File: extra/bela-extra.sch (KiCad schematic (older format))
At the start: 15 parts, among them P1 bbbp9, P14 ext_power, P2 bbbp8, P3 enc+btn1, P4 enc+btn2, P5 MTA-156-2, P6 bela_power, U2 7805-xnor

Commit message: working with enables on extra board
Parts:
- removed C1: 220uF, Capacitors_ThroughHole:C_Radial_D5_L11_P2, symbol CP
- removed C6: 47uF, Capacitors_ThroughHole:C_Radial_D5_L11_P2, symbol CP
- removed D1: 1N5400, Diodes_ThroughHole:Diode_DO-41_SOD81_Horizontal_RM10, symbol D
- removed P1: bbbp9, Pin_Headers:Pin_Header_Straight_2x08_Pitch2.54mm, symbol CONN_02X08
- removed P6: bela_power, mta-156:MTA-156-2, symbol CONN_01X02
- removed R4: bead, xnorman:Resistor_Vertical_RM5mm-xnor, symbol R
- removed U2: 7805-xnor, TO_SOT_Packages_THT:TO-220_Neutral123_Vertical_LargePads, symbol 7805-xnor
- added P1: bbbp9, Pin_Headers:Pin_Header_Straight_2x23_Pitch2.54mm, symbol CONN_02X23
- added R?: bead, xnorman:Resistor_Vertical_RM5mm-xnor, symbol R
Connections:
- net 5v: now also R?.2
- net beladigin6: no longer P2.12 (P12)
- net encin1-a: no longer P2.24 (P24)
- net encin1-b: no longer P2.22 (P22)
- net encin1-btn: no longer P2.20 (P20)
- net encin2-a: now also P1.16 (P16)
- net encin2-b: now also P1.14 (P14)
- net encin2-btn: now also P1.12 (P12)
- net bb-vfdCTRLenable: now reaches P2.14 (P14)
- net at R1.2: now also P1.4 (P4)
- net bb-vfdD7enable: no longer names the net of P2.32 (P32)
- new net: P1.5 (P5), R?.1
- new net bb-vfdDOUTenable: P2.12 (P12)
- no-connect marks 25 -> 23
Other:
- note added: "26 used by bela"
- note added: "WHY DIDN't Bela USE GPIO_26 Pin 14 for digital/io???? seems good.."
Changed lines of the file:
@@
 Text GLabel 9650 1250 2    60   Output ~ 0
 +15v
-$Comp
-L R R4
-U 1 1 58571EBD
-P 10350 3150
-F 0 "R4" V 10430 3150 50  0000 C CNN
-F 1 "bead" V 10350 3150 50  0000 C CNN
-F 2 "xnorman:Resistor_Vertical_RM5mm-xnor" V 10280 3150 50  0001 C CNN
-F 3 "" H 10350 3150 50  0000 C CNN
-	1    10350 3150
-	0    1    1    0
-$EndComp
-$Comp
-L CP C6
-U 1 1 58571F15
-P 9900 3350
-F 0 "C6" H 9925 3450 50  0000 L CNN
-F 1 "47uF" H 9925 3250 50  0000 L CNN
-F 2 "Capacitors_ThroughHole:C_Radial_D5_L11_P2" H 9938 3200 50  0001 C CNN
-F 3 "" H 9900 3350 50  0000 C CNN
-	1    9900 3350
-	1    0    0    -1
-$EndComp
-$Comp
-L CP C1
-U 1 1 58571F59
-P 8750 3350
-F 0 "C1" H 8775 3450 50  0000 L CNN
-F 1 "220uF" H 8775 3250 50  0000 L CNN
-F 2 "Capacitors_ThroughHole:C_Radial_D5_L11_P2" H 8788 3200 50  0001 C CNN
-F 3 "" H 8750 3350 50  0000 C CNN
-	1    8750 3350
-	1    0    0    -1
-$EndComp
-$Comp
-L D D1
-U 1 1 58571F9F
-P 8400 3150
-F 0 "D1" H 8400 3250 50  0000 C CNN
-F 1 "1N5400" H 8400 3050 50  0000 C CNN
-F 2 "Diodes_ThroughHole:Diode_DO-41_SOD81_Horizontal_RM10" H 8400 3150 50  0001 C CNN
-F 3 "" H 8400 3150 50  0000 C CNN
-	1    8400 3150
-	-1   0    0    -1
-$EndComp
-Text GLabel 7900 3150 0    60   Input ~ 0
-+15v
-$Comp
-L GND #PWR02
-U 1 1 58572336
-P 9200 3750
-F 0 "#PWR02" H 9200 3500 50  0001 C CNN
-F 1 "GND" H 9200 3600 50  0000 C CNN
-F 2 "" H 9200 3750 50  0000 C CNN
-F 3 "" H 9200 3750 50  0000 C CNN
-	1    9200 3750
-	1    0    0    -1
-$EndComp
-Text GLabel 10050 2950 1    60   Output ~ 0
-5v
-$Comp
-L CONN_01X02 P6
-U 1 1 58577BC4
-P 10800 3550
-F 0 "P6" H 10800 3700 50  0000 C CNN
-F 1 "bela_power" V 10900 3550 50  0000 C CNN
-F 2 "mta-156:MTA-156-2" H 10800 3550 50  0001 C CNN
-F 3 "" H 10800 3550 50  0000 C CNN
-	1    10800 3550
-	1    0    0    -1
-$EndComp
 $Sheet
 S 2300 650  1400 1350
@@
 	1    0    0    -1
 $EndComp
-Text GLabel 5300 5200 2    60   Output ~ 0
-bb-vfdD7enable
+Text GLabel 5300 4200 2    60   Output ~ 0
+bb-vfdDOUTenable
 Text GLabel 5350 5900 2    60   Output ~ 0
 bb-vfdD0
@@
 Text GLabel 4700 4200 0    60   Input ~ 0
 beladigin5
-Text GLabel 5300 4200 2    60   Input ~ 0
-beladigin6
 Text GLabel 5350 4400 2    60   Output ~ 0
 beladigout2
@@
 Text GLabel 5350 5100 2    60   Output ~ 0
 beladigout6
-Text GLabel 4700 5100 0    60   Output ~ 0
-beladigout7
 Text GLabel 2450 3800 2    60   Output ~ 0
 3.3v
@@
 Text GLabel 2150 4400 2    60   Input ~ 0
 encin2-a
-Text GLabel 5350 4700 2    60   Input ~ 0
+Text GLabel 6550 4400 2    60   Input ~ 0
 encin1-b
-Text GLabel 5350 4600 2    60   Input ~ 0
+Text GLabel 6550 4300 2    60   Input ~ 0
 encin1-btn
-Text GLabel 5350 4800 2    60   Input ~ 0
+Text GLabel 6550 4500 2    60   Input ~ 0
 encin1-a
-Text Notes 5900 4750 0    60   ~ 0
+Text Notes 7100 4450 0    60   ~ 0
 enc1 not mapped to bela digital
 Text Notes 2200 4100 0    60   ~ 0
@@
 NoConn ~ 1500 3700
 NoConn ~ 1500 3800
-NoConn ~ 1500 3900
 NoConn ~ 2000 3700
 NoConn ~ 2000 3900
@@
 NoConn ~ 5250 3800
 NoConn ~ 5250 3900
-NoConn ~ 5250 4300
 NoConn ~ 4750 4300
 NoConn ~ 4750 4500
@@
 NoConn ~ 5250 4900
 NoConn ~ 4750 5300
-$Comp
-L CONN_02X08 P1
-U 1 1 586DA958
-P 1750 4050
-F 0 "P1" H 1750 4500 50  0000 C CNN
-F 1 "bbbp9" V 1750 4050 50  0000 C CNN
-F 2 "Pin_Headers:Pin_Header_Straight_2x08_Pitch2.54mm" H 1750 2850 50  0001 C CNN
-F 3 "" H 1750 2850 50  0000 C CNN
-	1    1750 4050
-	1    0    0    -1
-$EndComp
 $Comp
 L PWR_FLAG #FLG05
@@
 $EndComp
 $Comp
-L 7805-xnor U2
-U 1 1 586E3B91
-P 9350 3200
-F 0 "U2" H 9500 3004 50  0000 C CNN
-F 1 "7805-xnor" H 9350 3400 50  0000 C CNN
-F 2 "TO_SOT_Packages_THT:TO-220_Neutral123_Vertical_LargePads" H 9350 3200 50  0001 C CNN
-F 3 "" H 9350 3200 50  0000 C CNN
-	1    9350 3200
-	1    0    0    -1
-$EndComp
-$Comp
 L PWR_FLAG #FLG06
 U 1 1 586F1ADD
@@
 	9350 1250 9650 1250
 Wire Wire Line
-	9350 3650 9350 3450
-Wire Wire Line
-	8750 3650 10000 3650
-Wire Wire Line
-	8750 3650 8750 3500
-Wire Wire Line
-	9900 3650 9900 3500
-Connection ~ 9350 3650
-Wire Wire Line
-	8550 3150 8950 3150
-Wire Wire Line
-	8750 3150 8750 3200
-Connection ~ 8750 3150
-Wire Wire Line
-	7900 3150 8250 3150
-Wire Wire Line
-	9200 3750 9200 3650
-Connection ~ 9200 3650
-Wire Wire Line
-	10550 3500 10600 3500
-Wire Wire Line
-	10600 3600 10000 3600
-Wire Wire Line
-	10000 3600 10000 3650
-Connection ~ 9900 3650
-Wire Wire Line
-	10500 3150 10550 3150
-Wire Wire Line
-	10550 3150 10550 3500
-Wire Wire Line
 	5250 3700 5800 3700
 Wire Wire Line
@@
 	5300 5300 5250 5300
 Wire Wire Line
-	5250 5200 5300 5200
-Wire Wire Line
 	4650 5200 4750 5200
 Wire Wire Line
@@
 Wire Wire Line
 	5250 4100 5300 4100
-Wire Wire Line
-	5250 4200 5300 4200
 Wire Wire Line
 	4700 4400 4750 4400
@@
 Wire Wire Line
 	2150 4400 2000 4400
-Wire Wire Line
-	5350 4600 5250 4600
-Wire Wire Line
-	5250 4700 5350 4700
-Wire Wire Line
-	5250 4800 5350 4800
 Connection ~ 9600 1250
 Wire Wire Line
@@
 Wire Wire Line
 	9600 1050 9600 1250
-Wire Wire Line
-	9750 3150 10200 3150
-Wire Wire Line
-	9900 3150 9900 3200
-Connection ~ 9900 3150
-Wire Wire Line
-	10050 2950 10050 3150
-Connection ~ 10050 3150
 Wire Wire Line
 	2400 3650 2400 3800
@@
 	-1   0    0    1
 $EndComp
+Text GLabel 5350 4300 2    60   Output ~ 0
+bb-vfdCTRLenable
+$Comp
+L CONN_02X23 P1
+U 1 1 589C11B1
+P 1750 4800
+F 0 "P1" H 1750 6000 50  0000 C CNN
+F 1 "bbbp9" V 1750 4800 50  0000 C CNN
+F 2 "Pin_Headers:Pin_Header_Straight_2x23_Pitch2.54mm" H 1750 3950 50  0001 C CNN
+F 3 "" H 1750 3950 50  0000 C CNN
+	1    1750 4800
+	1    0    0    -1
+$EndComp
+$Comp
+L R R?
+U 1 1 589C2A34
+P 1250 3900
+F 0 "R?" V 1330 3900 50  0000 C CNN
+F 1 "bead" V 1250 3900 50  0000 C CNN
+F 2 "xnorman:Resistor_Vertical_RM5mm-xnor" V 1180 3900 50  0001 C CNN
+F 3 "" H 1250 3900 50  0000 C CNN
+	1    1250 3900
+	0    1    1    0
+$EndComp
+Text GLabel 750  3900 0    60   Output ~ 0
+5v
+Wire Wire Line
+	750  3900 1100 3900
+Wire Wire Line
+	1500 3900 1400 3900
+$Comp
+L PWR_FLAG #FLG?
+U 1 1 589C2C34
+P 1000 3800
+F 0 "#FLG?" H 1000 3895 50  0001 C CNN
+F 1 "PWR_FLAG" H 1000 3980 50  0000 C CNN
+F 2 "" H 1000 3800 50  0000 C CNN
+F 3 "" H 1000 3800 50  0000 C CNN
+	1    1000 3800
+	1    0    0    -1
+$EndComp
+Wire Wire Line
+	1000 3800 1000 3900
+Connection ~ 1000 3900
+Text Notes 5350 4900 0    60   ~ 0
+26 used by bela
+Text GLabel 6900 4200 2    60   Input ~ 0
+beladigin6
+Wire Wire Line
+	5250 4200 5300 4200
+Wire Wire Line
+	5250 4300 5350 4300
+Text Notes 4150 3400 0    60   ~ 0
+WHY DIDN't Bela USE GPIO_26 Pin 14 for digital/io???? seems good..
+Text GLabel 4700 5100 0    60   Output ~ 0
+beladigout7
 $EndSCHEMATC

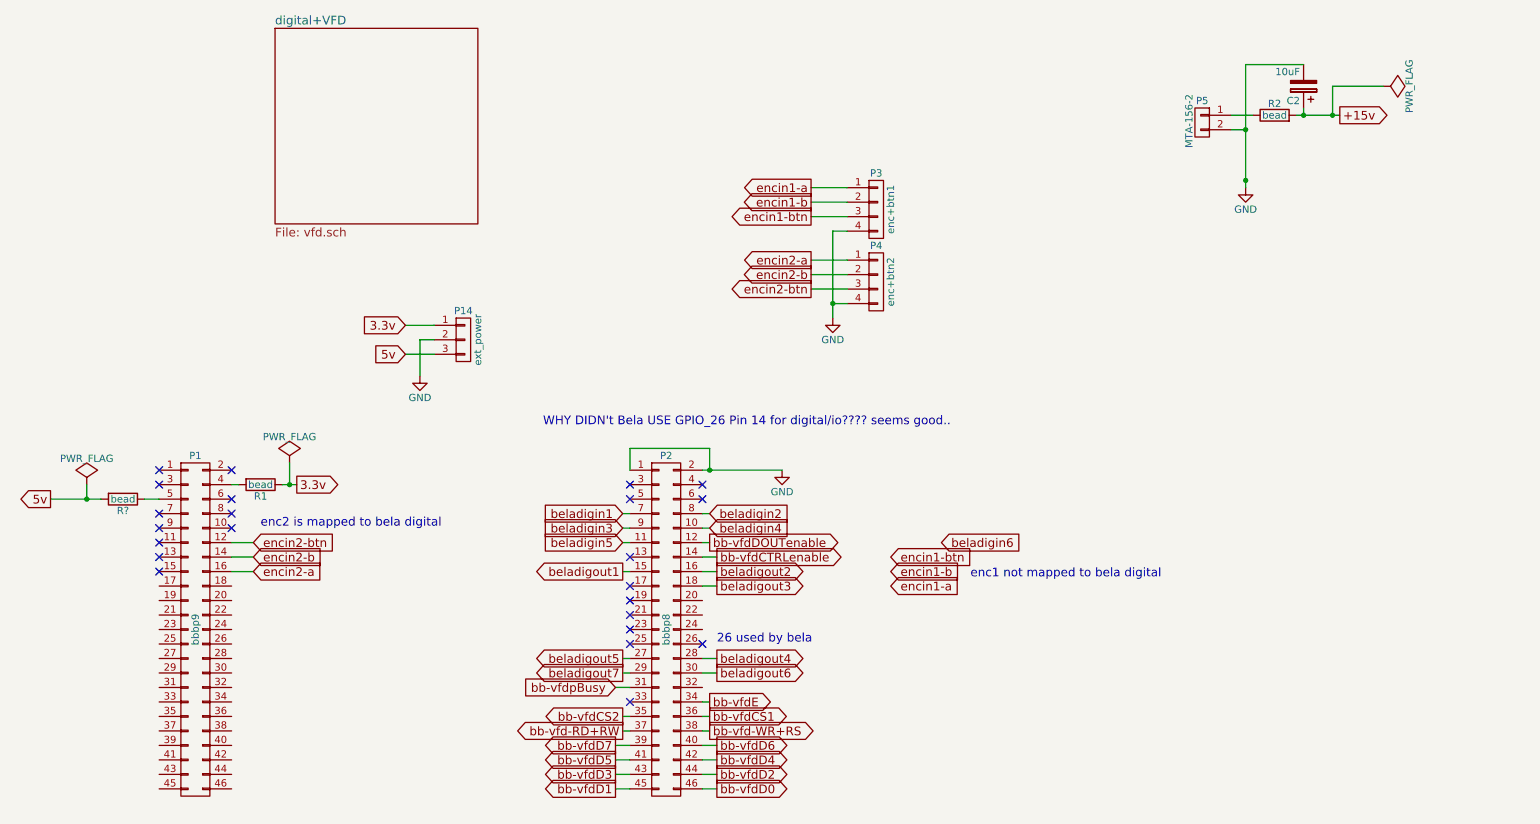
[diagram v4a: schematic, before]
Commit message: ditched power, remapped a bunch of io
should have all the emmc and lcd lines disabled at boot
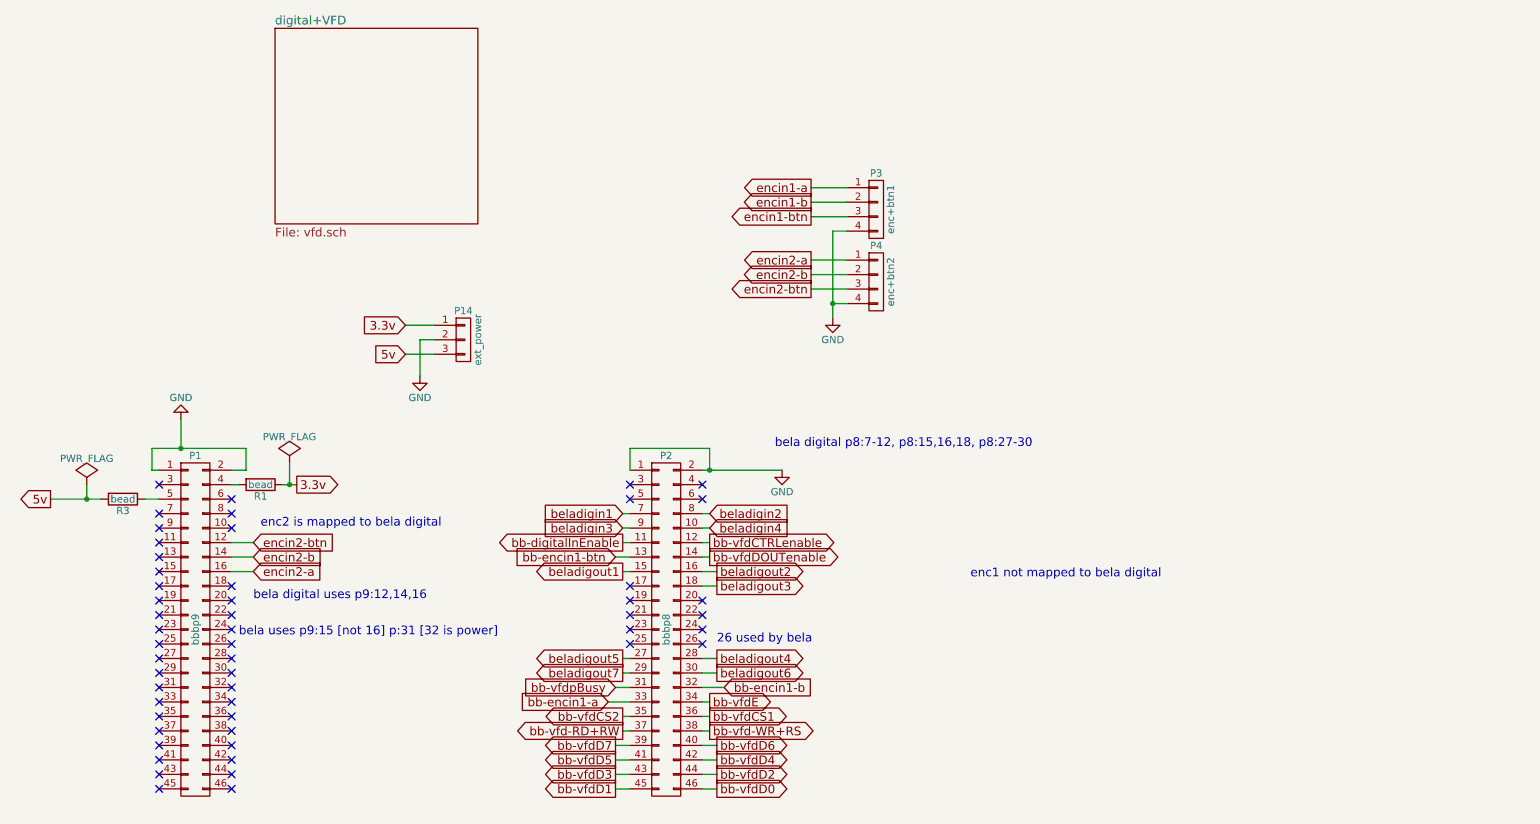
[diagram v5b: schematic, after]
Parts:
- removed C2: 10uF, Capacitors_ThroughHole:C_Radial_D5_L11_P2, symbol CP
- removed P5: MTA-156-2, mta-156:MTA-156-2, symbol MTA-156-2
- removed R2: bead, xnorman:Resistor_Vertical_RM5mm-xnor, symbol R
- gave numbers to parts that had none: 1
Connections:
- net GND: now also P1.1 (P1), P1.2 (P2)
- net bb-vfdCTRLenable: now also P2.12 (P12); no longer P2.14 (P14)
- net bb-vfdDOUTenable: now also P2.14 (P14); no longer P2.12 (P12)
- net bb-encin1-btn: now reaches P2.13 (P13)
- net bb-encin1-b: now reaches P2.32 (P32)
- net bb-encin1-a: now reaches P2.33 (P33)
- net beladigin5 renamed bb-digitalInEnable
- no-connect marks 23 -> 52
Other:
- note added: "bela digital p8:7-12, p8:15,16,18, p8:27-30"
- note added: "bela digital uses p9:12,14,16"
- note added: "bela uses p9:15 [not 16] p:31 [32 is power]"
- note removed: "WHY DIDN't Bela USE GPIO_26 Pin 14 for digital/io???? seems good.."
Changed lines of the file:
@@
 Comment4 ""
 $EndDescr
-$Comp
-L R R2
-U 1 1 58571AB6
-P 9200 1250
-F 0 "R2" V 9280 1250 50  0000 C CNN
-F 1 "bead" V 9200 1250 50  0000 C CNN
-F 2 "xnorman:Resistor_Vertical_RM5mm-xnor" V 9130 1250 50  0001 C CNN
-F 3 "" H 9200 1250 50  0000 C CNN
-	1    9200 1250
-	0    -1   -1   0
-$EndComp
-$Comp
-L GND #PWR01
-U 1 1 58571AB8
-P 9000 1750
-F 0 "#PWR01" H 9000 1500 50  0001 C CNN
-F 1 "GND" H 9000 1600 50  0000 C CNN
-F 2 "" H 9000 1750 50  0000 C CNN
-F 3 "" H 9000 1750 50  0000 C CNN
-	1    9000 1750
-	1    0    0    -1
-$EndComp
-Text GLabel 9650 1250 2    60   Output ~ 0
-+15v
 $Sheet
 S 2300 650  1400 1350
@@
 $EndComp
 $Comp
-L GND #PWR03
+L GND #PWR01
 U 1 1 586B08A6
 P 5800 3700
-F 0 "#PWR03" H 5800 3450 50  0001 C CNN
+F 0 "#PWR01" H 5800 3450 50  0001 C CNN
 F 1 "GND" H 5800 3550 50  0000 C CNN
 F 2 "" H 5800 3700 50  0000 C CNN
@@
 	1    0    0    -1
 $EndComp
-Text GLabel 5300 4200 2    60   Output ~ 0
+Text GLabel 5300 4300 2    60   Output ~ 0
 bb-vfdDOUTenable
 Text GLabel 5350 5900 2    60   Output ~ 0
@@
 Text GLabel 5300 4100 2    60   Input ~ 0
 beladigin4
-Text GLabel 4700 4200 0    60   Input ~ 0
-beladigin5
 Text GLabel 5350 4400 2    60   Output ~ 0
 beladigout2
@@
 encin2-a
 $Comp
-L GND #PWR04
+L GND #PWR02
 U 1 1 586C8041
 P 6150 2650
-F 0 "#PWR04" H 6150 2400 50  0001 C CNN
+F 0 "#PWR02" H 6150 2400 50  0001 C CNN
 F 1 "GND" H 6150 2500 50  0000 C CNN
 F 2 "" H 6150 2650 50  0000 C CNN
@@
 Text GLabel 2150 4400 2    60   Input ~ 0
 encin2-a
-Text GLabel 6550 4400 2    60   Input ~ 0
-encin1-b
-Text GLabel 6550 4300 2    60   Input ~ 0
-encin1-btn
-Text GLabel 6550 4500 2    60   Input ~ 0
-encin1-a
+Text GLabel 5400 5200 2    60   Input ~ 0
+bb-encin1-b
+Text GLabel 4650 4300 0    60   Input ~ 0
+bb-encin1-btn
+Text GLabel 4600 5300 0    60   Input ~ 0
+bb-encin1-a
 Text Notes 7100 4450 0    60   ~ 0
 enc1 not mapped to bela digital
 Text Notes 2200 4100 0    60   ~ 0
 enc2 is mapped to bela digital
-NoConn ~ 1500 3700
 NoConn ~ 1500 3800
-NoConn ~ 2000 3700
 NoConn ~ 2000 3900
 NoConn ~ 2000 4000
@@
 NoConn ~ 5250 3800
 NoConn ~ 5250 3900
-NoConn ~ 4750 4300
 NoConn ~ 4750 4500
 NoConn ~ 4750 4600
@@
 NoConn ~ 4750 4900
 NoConn ~ 5250 4900
-NoConn ~ 4750 5300
-$Comp
-L PWR_FLAG #FLG05
-U 1 1 586DBA15
-P 9950 1050
-F 0 "#FLG05" H 9950 1145 50  0001 C CNN
-F 1 "PWR_FLAG" H 9950 1230 50  0000 C CNN
-F 2 "" H 9950 1050 50  0000 C CNN
-F 3 "" H 9950 1050 50  0000 C CNN
-	1    9950 1050
-	0    1    1    0
-$EndComp
-$Comp
-L PWR_FLAG #FLG06
+$Comp
+L PWR_FLAG #FLG03
 U 1 1 586F1ADD
 P 2400 3650
-F 0 "#FLG06" H 2400 3745 50  0001 C CNN
+F 0 "#FLG03" H 2400 3745 50  0001 C CNN
 F 1 "PWR_FLAG" H 2400 3830 50  0000 C CNN
 F 2 "" H 2400 3650 50  0000 C CNN
@@
 5v
 $Comp
-L GND #PWR07
+L GND #PWR04
 U 1 1 5871F064
 P 3300 3050
-F 0 "#PWR07" H 3300 2800 50  0001 C CNN
+F 0 "#PWR04" H 3300 2800 50  0001 C CNN
 F 1 "GND" H 3300 2900 50  0000 C CNN
 F 2 "" H 3300 3050 50  0000 C CNN
@@
 	1    0    0    -1
 $EndComp
-$Comp
-L MTA-156-2 P5
-U 1 1 58726CA4
-P 8700 1400
-F 0 "P5" H 8700 1650 50  0000 C CNN
-F 1 "MTA-156-2" V 8790 1510 50  0000 C CNN
-F 2 "mta-156:MTA-156-2" H 8700 1400 50  0001 C CNN
-F 3 "" H 8700 1400 50  0000 C CNN
-	1    8700 1400
-	-1   0    0    -1
-$EndComp
-Wire Wire Line
-	8900 1250 9050 1250
-Wire Wire Line
-	9350 1250 9650 1250
 Wire Wire Line
 	5250 3700 5800 3700
@@
 	5250 5400 5300 5400
 Wire Wire Line
-	5300 5300 5250 5300
-Wire Wire Line
 	4650 5200 4750 5200
 Wire Wire Line
@@
 Wire Wire Line
 	4700 4100 4750 4100
-Wire Wire Line
-	4700 4200 4750 4200
 Wire Wire Line
 	5250 4000 5300 4000
@@
 Wire Wire Line
 	2150 4400 2000 4400
-Connection ~ 9600 1250
-Wire Wire Line
-	9950 1050 9600 1050
-Wire Wire Line
-	9600 1050 9600 1250
 Wire Wire Line
 	2400 3650 2400 3800
@@
 Wire Wire Line
 	3300 2800 3300 3050
-Connection ~ 9000 1700
-Wire Wire Line
-	8900 1350 9000 1350
-Connection ~ 9400 1250
-Wire Wire Line
-	9400 1200 9400 1250
-Connection ~ 9000 1350
-Wire Wire Line
-	9000 900  9000 1750
-Wire Wire Line
-	9400 900  9000 900
-$Comp
-L CP C2
-U 1 1 58571ABA
-P 9400 1050
-F 0 "C2" H 9425 1150 50  0000 L CNN
-F 1 "10uF" H 9425 950 50  0000 L CNN
-F 2 "Capacitors_ThroughHole:C_Radial_D5_L11_P2" H 9438 900 50  0001 C CNN
-F 3 "" H 9400 1050 50  0000 C CNN
-	1    9400 1050
-	-1   0    0    1
-$EndComp
-Text GLabel 5350 4300 2    60   Output ~ 0
+Text GLabel 5300 4200 2    60   Output ~ 0
 bb-vfdCTRLenable
 $Comp
@@
 $EndComp
 $Comp
-L R R?
+L R R3
 U 1 1 589C2A34
 P 1250 3900
-F 0 "R?" V 1330 3900 50  0000 C CNN
+F 0 "R3" V 1330 3900 50  0000 C CNN
 F 1 "bead" V 1250 3900 50  0000 C CNN
 F 2 "xnorman:Resistor_Vertical_RM5mm-xnor" V 1180 3900 50  0001 C CNN
@@
 	1500 3900 1400 3900
 $Comp
-L PWR_FLAG #FLG?
+L PWR_FLAG #FLG05
 U 1 1 589C2C34
 P 1000 3800
-F 0 "#FLG?" H 1000 3895 50  0001 C CNN
+F 0 "#FLG05" H 1000 3895 50  0001 C CNN
 F 1 "PWR_FLAG" H 1000 3980 50  0000 C CNN
 F 2 "" H 1000 3800 50  0000 C CNN
@@
 Text Notes 5350 4900 0    60   ~ 0
 26 used by bela
-Text GLabel 6900 4200 2    60   Input ~ 0
-beladigin6
-Wire Wire Line
-	5250 4200 5300 4200
-Wire Wire Line
-	5250 4300 5350 4300
-Text Notes 4150 3400 0    60   ~ 0
-WHY DIDN't Bela USE GPIO_26 Pin 14 for digital/io???? seems good..
 Text GLabel 4700 5100 0    60   Output ~ 0
 beladigout7
+Text GLabel 4700 4200 0    60   Output ~ 0
+bb-digitalInEnable
+Text Notes 2050 4850 0    60   ~ 0
+bela uses p9:15 [not 16] p:31 [32 is power]
+Wire Wire Line
+	4750 4200 4700 4200
+Wire Wire Line
+	5250 4200 5300 4200
+Wire Wire Line
+	5250 4300 5300 4300
+Text Notes 5750 3550 0    60   ~ 0
+bela digital p8:7-12, p8:15,16,18, p8:27-30
+Text Notes 2150 4600 0    60   ~ 0
+bela digital uses p9:12,14,16
+Wire Wire Line
+	4750 4300 4650 4300
+Wire Wire Line
+	4750 5300 4600 5300
+Wire Wire Line
+	5300 5300 5250 5300
+Wire Wire Line
+	5400 5200 5250 5200
+NoConn ~ 2000 4500
+NoConn ~ 2000 4600
+NoConn ~ 1500 4500
+NoConn ~ 1500 4600
+NoConn ~ 1500 4700
+NoConn ~ 1500 4800
+NoConn ~ 1500 4900
+NoConn ~ 1500 5000
+NoConn ~ 1500 5100
+NoConn ~ 1500 5200
+NoConn ~ 1500 5300
+NoConn ~ 1500 5400
+NoConn ~ 1500 5500
+NoConn ~ 1500 5600
+NoConn ~ 1500 5700
+NoConn ~ 1500 5800
+NoConn ~ 1500 5900
+NoConn ~ 2000 5900
+NoConn ~ 2000 5800
+NoConn ~ 2000 5700
+NoConn ~ 2000 5600
+NoConn ~ 2000 5500
+NoConn ~ 2000 5400
+NoConn ~ 2000 5300
+NoConn ~ 2000 5200
+NoConn ~ 2000 5100
+NoConn ~ 2000 5000
+NoConn ~ 2000 4900
+NoConn ~ 2000 4800
+NoConn ~ 2000 4700
+NoConn ~ 5250 4600
+NoConn ~ 5250 4700
+NoConn ~ 5250 4800
+Wire Wire Line
+	2000 3700 2100 3700
+Wire Wire Line
+	2100 3700 2100 3550
+Wire Wire Line
+	2100 3550 1450 3550
+Wire Wire Line
+	1450 3550 1450 3700
+Wire Wire Line
+	1450 3700 1500 3700
+$Comp
+L GND #PWR?
+U 1 1 58A03A53
+P 1650 3350
+F 0 "#PWR?" H 1650 3100 50  0001 C CNN
+F 1 "GND" H 1650 3200 50  0000 C CNN
+F 2 "" H 1650 3350 50  0000 C CNN
+F 3 "" H 1650 3350 50  0000 C CNN
+	1    1650 3350
+	-1   0    0    1
+$EndComp
+Wire Wire Line
+	1650 3350 1650 3550
+Connection ~ 1650 3550
 $EndSCHEMATC
